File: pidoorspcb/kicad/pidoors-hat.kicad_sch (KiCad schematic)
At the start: 0 parts

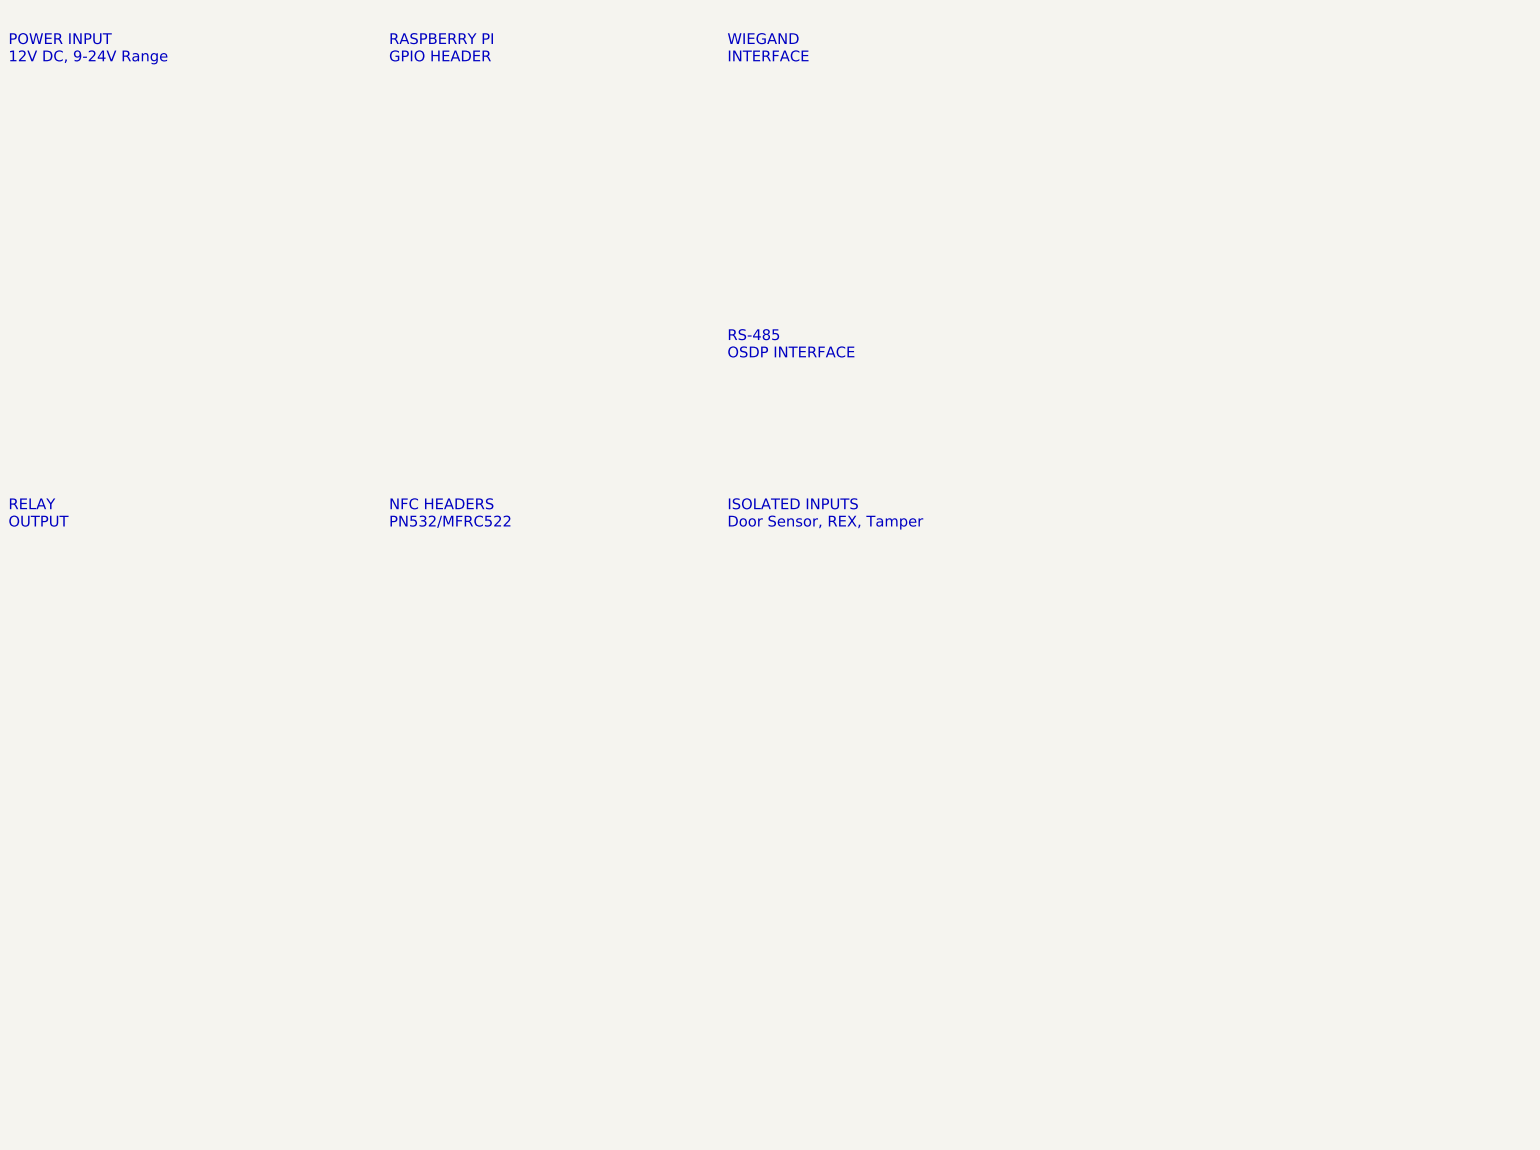
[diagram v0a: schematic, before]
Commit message: PCB: Complete routing and generate Gerber manufacturing files
- Fix GPIO discrepancy: LED Granted now uses GPIO 25 (was GPIO 5)
- Fix README: Relay uses GPIO 18 (was incorrectly listed as GPIO 17)
- Complete KiCad schematic with all component symbols and connections
- Route PCB with power traces (0.5mm) and signal traces (0.25mm)
- Add ground plane on bottom copper layer
- Generate Gerber files in RS-274X format for JLCPCB
- Generate Excellon drill files (PTH and NPTH)
- Add manufacturing checklist with ordering instructions
- Add gerber generation script for KiCad 8.x

Co-Authored-By: Claude Opus 4.5 <noreply@anthropic.com>
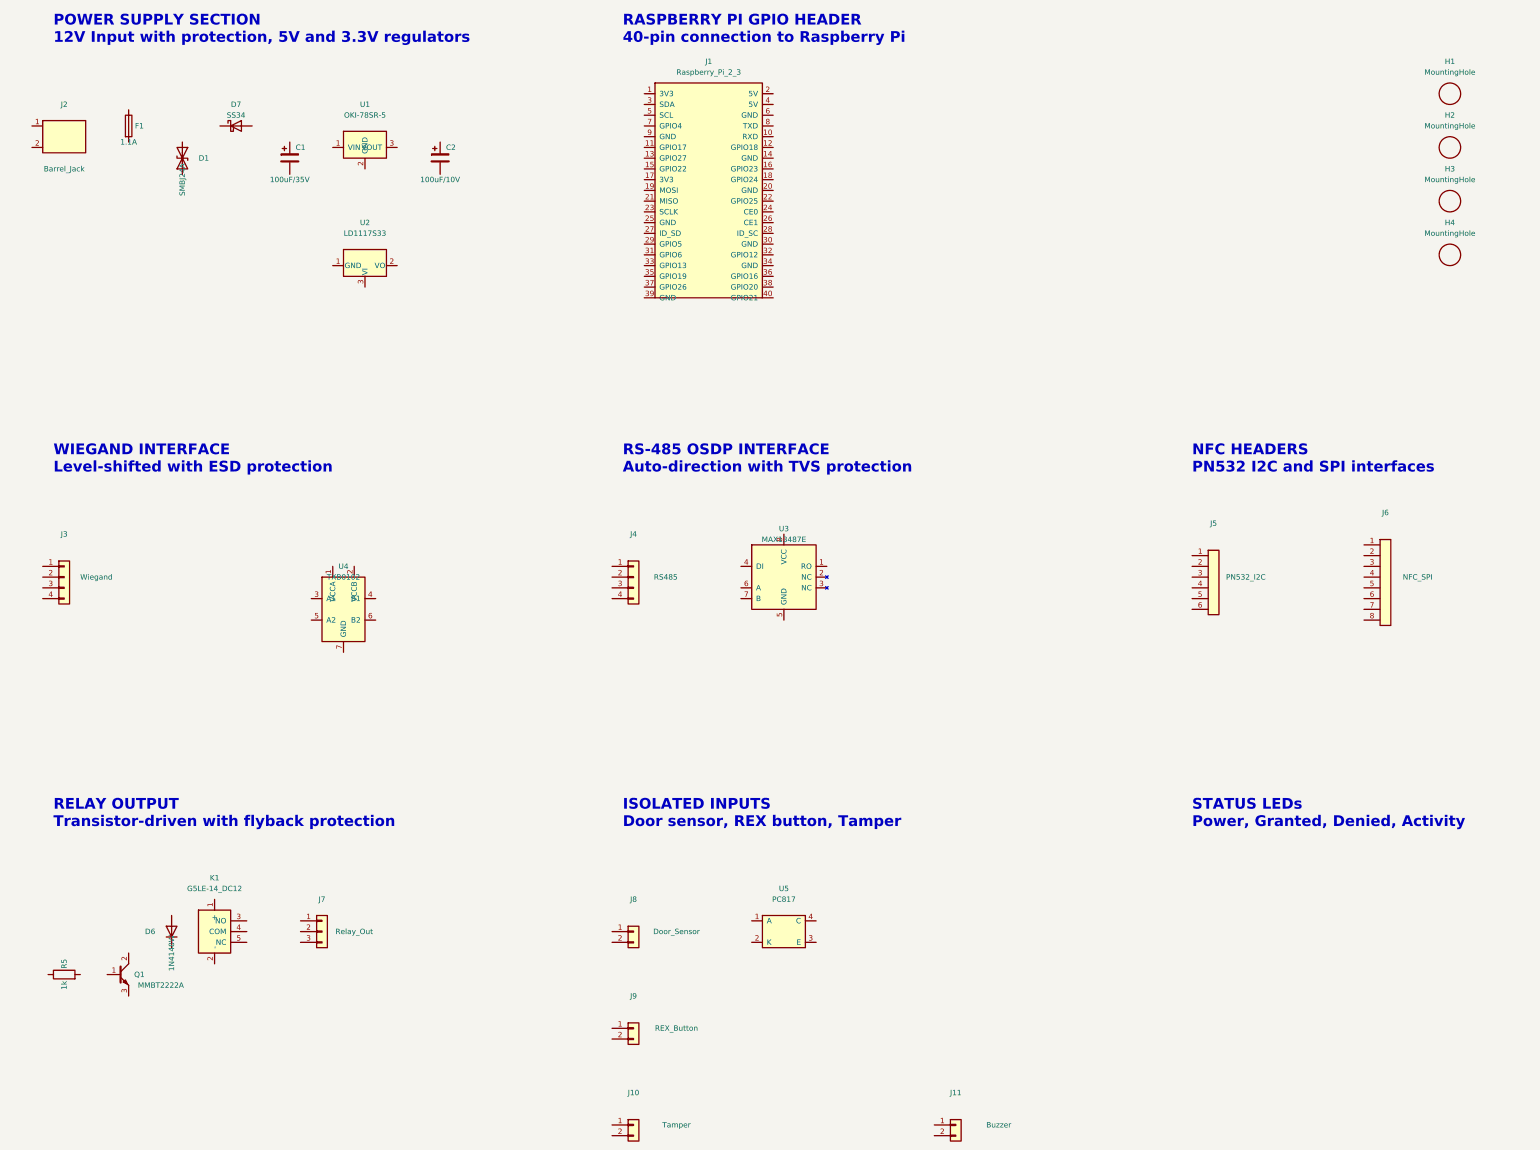
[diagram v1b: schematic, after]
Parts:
- added C1: 100uF/35V, Capacitor_THT:CP_Radial_D8.0mm_P3.50mm, symbol Device:CP
- added C2: 100uF/10V, Capacitor_THT:CP_Radial_D6.3mm_P2.50mm, symbol Device:CP
- added D1: SMBJ24A, Diode_SMD:D_SMB, symbol Device:D_TVS
- added D6: 1N4148W, Diode_SMD:D_SOD-123, symbol Device:D
- added D7: SS34, Diode_SMD:D_SMA, symbol Device:D_Schottky
- added F1: 1.1A, Fuse:Fuse_1812_4532Metric, symbol Device:Fuse
- added H1, H2, H3, H4: MountingHole, MountingHole:MountingHole_2.7mm_M2.5, symbol Mechanical:MountingHole
- added J1: Raspberry_Pi_2_3, Connector_PinSocket_2.54mm:PinSocket_2x20_P2.54mm_Vertical, symbol Connector:Raspberry_Pi_2_3
- added J10: Tamper, Connector_PinHeader_2.54mm:PinHeader_1x02_P2.54mm_Vertical, symbol Connector_Generic:Conn_01x02
- added J11: Buzzer, TerminalBlock_Phoenix:TerminalBlock_Phoenix_MKDS-1,5-2-5.08_1x02_P5.08mm_Horizontal, symbol Connector_Generic:Conn_01x02
- added J2: Barrel_Jack, Connector_BarrelJack:BarrelJack_CUI_PJ-002A_Horizontal, symbol Connector:Barrel_Jack_Switch
- added J3: Wiegand, TerminalBlock_Phoenix:TerminalBlock_Phoenix_MKDS-1,5-4-5.08_1x04_P5.08mm_Horizontal, symbol Connector_Generic:Conn_01x04
- added J4: RS485, TerminalBlock_Phoenix:TerminalBlock_Phoenix_MKDS-1,5-4-5.08_1x04_P5.08mm_Horizontal, symbol Connector_Generic:Conn_01x04
- added J5: PN532_I2C, Connector_PinHeader_2.54mm:PinHeader_1x06_P2.54mm_Vertical, symbol Connector_Generic:Conn_01x06
- added J6: NFC_SPI, Connector_PinHeader_2.54mm:PinHeader_1x08_P2.54mm_Vertical, symbol Connector_Generic:Conn_01x08
- added J7: Relay_Out, TerminalBlock_Phoenix:TerminalBlock_Phoenix_MKDS-1,5-3-5.08_1x03_P5.08mm_Horizontal, symbol Connector_Generic:Conn_01x03
- added J8: Door_Sensor, TerminalBlock_Phoenix:TerminalBlock_Phoenix_MKDS-1,5-2-5.08_1x02_P5.08mm_Horizontal, symbol Connector_Generic:Conn_01x02
- added J9: REX_Button, TerminalBlock_Phoenix:TerminalBlock_Phoenix_MKDS-1,5-2-5.08_1x02_P5.08mm_Horizontal, symbol Connector_Generic:Conn_01x02
- added K1: G5LE-14_DC12, Relay_THT:Relay_SPDT_Omron-G5LE-14, symbol Relay:G5LE-14
- added Q1: MMBT2222A, Package_TO_SOT_SMD:SOT-23, symbol Transistor_BJT:MMBT2222A
- added R5: 1k, Resistor_SMD:R_0603_1608Metric, symbol Device:R
- added U1: OKI-78SR-5, Converter_DCDC:Converter_DCDC_muRata_OKI-78SRx_Vertical, symbol Converter_DCDC:OKI-78SR-5
- added U2: LD1117S33, Package_TO_SOT_SMD:SOT-223-3_TabPin2, symbol Regulator_Linear:LD1117S33TR_SOT223
- added U3: MAX13487E, Package_SO:SOIC-8_3.9x4.9mm_P1.27mm, symbol Interface_UART:MAX13487E
- added U4: TXB0102, Package_TO_SOT_SMD:SOT-23-6, symbol Logic_LevelTranslator:TXB0102
- added U5: PC817, Package_DIP:DIP-4_W7.62mm, symbol Isolator:PC817
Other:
- note added: "ISOLATED INPUTS Door sensor, REX button, Tamper"
- note added: "NFC HEADERS PN532 I2C and SPI interfaces"
- note added: "POWER SUPPLY SECTION 12V Input with protection, 5V and 3.3V regulators"
- note added: "RASPBERRY PI GPIO HEADER 40-pin connection to Raspberry Pi"
- note added: "RELAY OUTPUT Transistor-driven with flyback protection"
- note added: "RS-485 OSDP INTERFACE Auto-direction with TVS protection"
- note added: "STATUS LEDs Power, Granted, Denied, Activity"
- note added: "WIEGAND INTERFACE Level-shifted with ESD protection"
- note removed: "ISOLATED INPUTS Door Sensor, REX, Tamper"
- note removed: "NFC HEADERS PN532/MFRC522"
- note removed: "POWER INPUT 12V DC, 9-24V Range"
- note removed: "RASPBERRY PI GPIO HEADER"
- note removed: "RELAY OUTPUT"
- note removed: "RS-485 OSDP INTERFACE"
- note removed: "WIEGAND INTERFACE"
